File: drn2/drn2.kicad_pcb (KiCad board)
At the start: 2 copper layers, 123 x 89 mm, 54 parts, among them J1 Conn_01x03_Socket, J10 Conn_01x03_Socket, J11 Conn_01x03_Socket, J12 Conn_01x03_Socket, J13 Conn_01x03_Socket, J14 Conn_01x03_Socket, J15 Conn_01x03_Socket, J16 Conn_01x03_Socket, J2 Raspberry_Pi_2_3, J3 Conn_01x03_Socket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

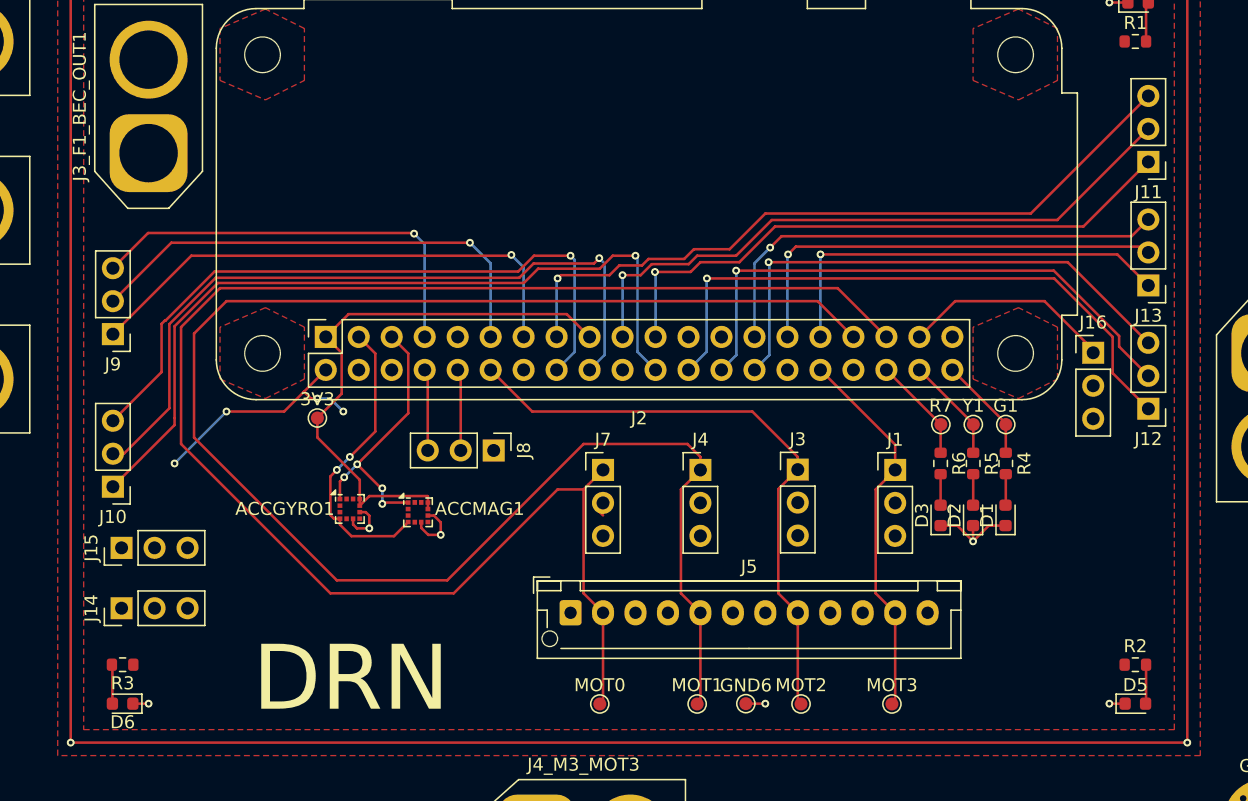
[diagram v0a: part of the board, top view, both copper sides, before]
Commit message: feat: pcb version 2.8
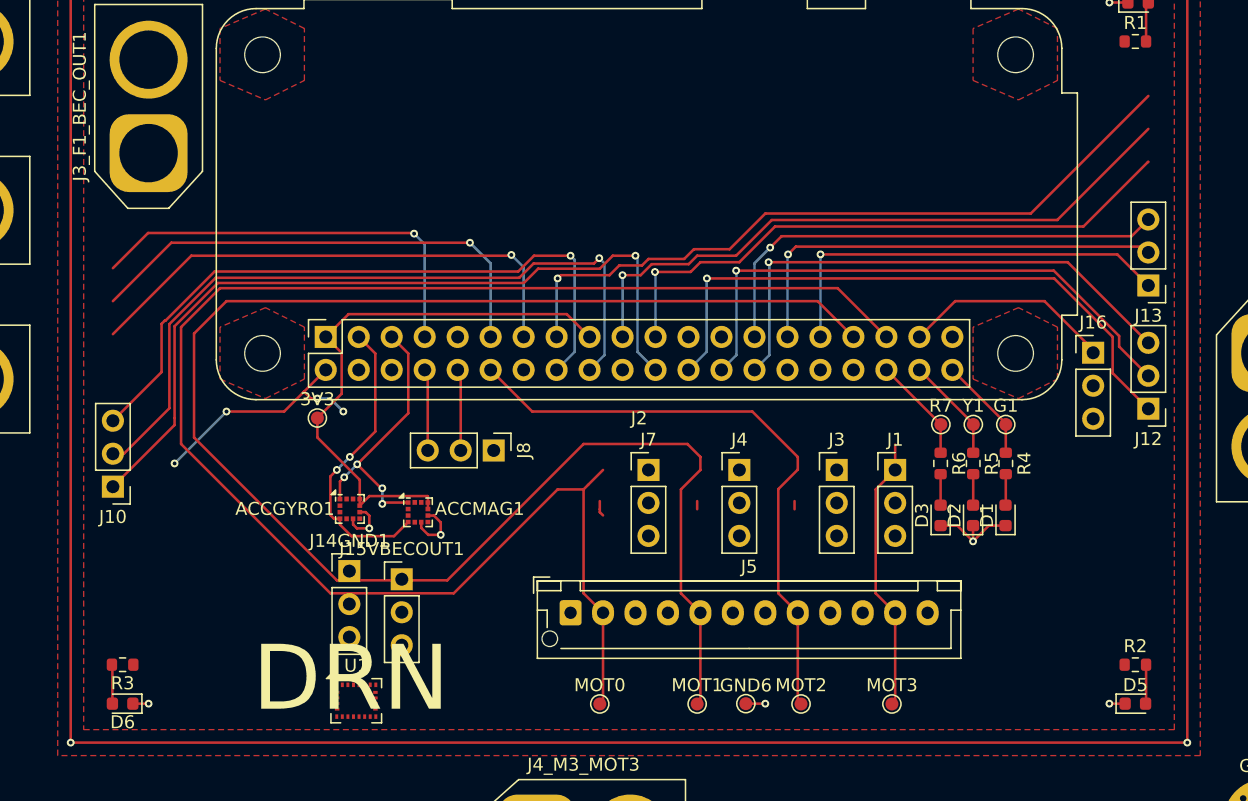
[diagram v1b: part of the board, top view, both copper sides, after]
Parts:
- removed J11, J14, J15, J9: Conn_01x03_Socket, Connector_PinHeader_2.54mm:PinHeader_1x03_P2.54mm_Vertical
- added J14GND1: Conn_01x03_Socket, Connector_PinHeader_2.54mm:PinHeader_1x03_P2.54mm_Vertical, F.Cu at (103.5, 87.8)
- added J15VBECOUT1: Conn_01x03_Socket, Connector_PinHeader_2.54mm:PinHeader_1x03_P2.54mm_Vertical, F.Cu at (107.5, 88.4)
- added U1: LSM9DS1, Package_LGA:LGA-24L_3x3.5mm_P0.43mm, F.Cu at (104.0, 97.8)
- moved J7 3.50 mm to (126.5, 80.0)
- moved J3 3.00 mm to (141.0, 80.0)
- moved J4 3.00 mm to (133.5, 80.0)
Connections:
- J10 pad 1: Net-(J10-Pin_1) -> unconnected-(J10-Pin_1-Pad1)
- J10 pad 2: Net-(J10-Pin_2) -> unconnected-(J10-Pin_2-Pad2)
- J10 pad 3: Net-(J10-Pin_3) -> unconnected-(J10-Pin_3-Pad3)
- J12 pad 1: Net-(J12-Pin_1) -> unconnected-(J12-Pin_1-Pad1)
- J12 pad 2: Net-(J12-Pin_2) -> unconnected-(J12-Pin_2-Pad2)
- J12 pad 3: Net-(J12-Pin_3) -> unconnected-(J12-Pin_3-Pad3)
- J16 pad 1: Net-(J16-Pin_1) -> /GND
- J16 pad 3: /GND -> Net-(J16-Pin_3)
- J2 pad 16: Net-(J10-Pin_3) -> Net-(J2-GPIO23)
- J2 pad 18: Net-(J10-Pin_2) -> Net-(J2-GPIO24)
- J2 pad 22: Net-(J10-Pin_1) -> unconnected-(J2-GPIO25-Pad22)
- J2 pad 23: unconnected-(J2-SCLK0/GPIO11-Pad23) -> Net-(J2-SCLK0/GPIO11)
- J2 pad 24: Net-(J12-Pin_1) -> unconnected-(J2-~{CE0}/GPIO8-Pad24)
- J2 pad 26: Net-(J12-Pin_2) -> unconnected-(J2-~{CE1}/GPIO7-Pad26)
- J2 pad 27: Net-(J13-Pin_3) -> Net-(J13-Pin_1)
- J2 pad 28: Net-(J12-Pin_3) -> unconnected-(J2-ID_SC/GPIO1-Pad28)
- J2 pad 31: Net-(J13-Pin_1) -> Net-(J13-Pin_3)
- J2 pad 32: Net-(J1-Pin_1) -> Net-(J2-PWM0/GPIO12)
- J2 pad 35: Net-(J2-GPIO19/MISO1) -> Net-(J1-Pin_1)
- J2 pad 37: Net-(J16-Pin_1) -> Net-(J16-Pin_3)
- J3 pad 1: Net-(J2-GPIO18/PWM0) -> Net-(J2-PWM1/GPIO13)
- J4 pad 1: Net-(J2-PWM1/GPIO13) -> Net-(J2-PWM0/GPIO12)
- J5 pad 2: Net-(J2-GPIO19/MISO1) -> Net-(J2-GPIO18/PWM0)
- J5 pad 5: Net-(J2-PWM1/GPIO13) -> Net-(J2-PWM0/GPIO12)
- J5 pad 8: Net-(J2-GPIO18/PWM0) -> Net-(J2-PWM1/GPIO13)
- J7 pad 1: Net-(J2-GPIO19/MISO1) -> Net-(J2-GPIO18/PWM0)
- MOT0 pad 1: Net-(J2-GPIO19/MISO1) -> Net-(J1-Pin_1)
- MOT2 pad 1: Net-(J2-GPIO18/PWM0) -> Net-(J2-PWM0/GPIO12)
- MOT3 pad 1: Net-(J1-Pin_1) -> Net-(J2-GPIO18/PWM0)
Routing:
- net (no net): track 0.00 -> 426.8 mm, vias 0 -> 6
- net Net-(J2-GPIO19/MISO1): track 124.6 -> 0.00 mm
- net Net-(J10-Pin_1): track 61.5 -> 0.00 mm, vias 1 -> 0
- net Net-(J10-Pin_2): track 56.7 -> 0.00 mm, vias 1 -> 0
- net Net-(J10-Pin_3): track 52.2 -> 0.00 mm, vias 1 -> 0
- net Net-(J12-Pin_1): track 47.4 -> 0.00 mm, vias 1 -> 0
- net Net-(J12-Pin_2): track 43.7 -> 0.00 mm, vias 1 -> 0
- net Net-(J12-Pin_3): track 40.6 -> 0.00 mm, vias 1 -> 0
- net /GND: track 24.0 -> 40.3 mm
- net Net-(J16-Pin_1): track 16.3 -> 0.00 mm
- net Net-(J1-Pin_1): track 29.5 -> 21.3 mm

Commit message: feat: pcb v3
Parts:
- removed 3V3: TestPoint, TestPoint:TestPoint_Pad_D1.0mm
- removed ACCGYRO1: LSM6, Package_LGA:LGA-12_2x2mm_P0.5mm
- removed ACCMAG1: LSM303, Package_LGA:LGA-12_2x2mm_P0.5mm
- removed J10: Conn_01x03_Socket, Connector_PinHeader_2.54mm:PinHeader_1x03_P2.54mm_Vertical
- added C1: 100nF, Capacitor_SMD:C_0603_1608Metric_Pad1.08x0.95mm_HandSolder, F.Cu at (117.0, 83.5)
- added C2: 100nF, Capacitor_SMD:C_0603_1608Metric_Pad1.08x0.95mm_HandSolder, F.Cu at (118.7, 81.7)
- added C3: 100nF, Capacitor_SMD:C_0603_1608Metric_Pad1.08x0.95mm_HandSolder, F.Cu at (115.0, 83.5)
- added C4: C_Polarized, Capacitor_SMD:CP_Elec_4x5.4, F.Cu at (109.5, 80.5)
- added C5: 10nF, Capacitor_SMD:C_0603_1608Metric_Pad1.08x0.95mm_HandSolder, F.Cu at (113.0, 83.5)
- added R10: 130, Resistor_SMD:R_0603_1608Metric, F.Cu at (110.0, 85.0)
- added R11: 130, Resistor_SMD:R_0603_1608Metric, F.Cu at (121.5, 83.0)
- added R8: 130, Resistor_SMD:R_0603_1608Metric, F.Cu at (106.5, 85.0)
- added R9: 130, Resistor_SMD:R_0603_1608Metric, F.Cu at (121.5, 80.0)
- added VDD1: TestPoint, TestPoint:TestPoint_Pad_D1.0mm, F.Cu at (103.5, 82.4)
- added VDDIO1: TestPoint, TestPoint:TestPoint_Pad_D1.0mm, F.Cu at (125.4, 83.0)
- moved J8 29.5 mm to (89.5, 63.0), turned to 0 degrees
- moved U1 22.2 mm to (115.6, 78.9), turned to 180 degrees
- moved J14GND1 8.89 mm to (111.0, 92.5)
- moved J15VBECOUT1 8.53 mm to (115.0, 92.5)
- moved J7 5.40 mm to (131.9, 80.1)
- moved J13 5.32 mm to (165.0, 60.5), turned to 0 degrees
- moved J16 5.07 mm to (160.8, 76.0), turned to 180 degrees
- moved J12 4.32 mm to (165.0, 71.0), turned to 0 degrees
- moved J4 3.00 mm to (136.5, 80.0)
- moved MOT0 0.25 mm to (145.5, 98.0)
- moved MOT1 0.25 mm to (138.0, 98.0)
- moved MOT2 0.25 mm to (130.5, 98.0)
- moved MOT3 0.25 mm to (123.0, 98.0)
- renumbered MOT3 to MOT0, MOT2 to MOT1, MOT1 to MOT2, MOT0 to MOT3
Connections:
- net /3.3 renamed Net-(J2-3V3-Pad1)
- net /GND renamed GND
- J12 pad 1: unconnected-(J12-Pin_1-Pad1) -> Net-(J12-Pin_1)
- J12 pad 2: unconnected-(J12-Pin_2-Pad2) -> Net-(J12-Pin_2)
- J12 pad 3: unconnected-(J12-Pin_3-Pad3) -> Net-(J12-Pin_3)
- J2 pad 24: unconnected-(J2-~{CE0}/GPIO8-Pad24) -> Net-(J13-Pin_1)
- J2 pad 26: unconnected-(J2-~{CE1}/GPIO7-Pad26) -> Net-(J13-Pin_2)
- J2 pad 27: Net-(J13-Pin_1) -> Net-(J13-Pin_3)
- J2 pad 28: unconnected-(J2-ID_SC/GPIO1-Pad28) -> Net-(J12-Pin_1)
- J2 pad 29: Net-(J13-Pin_2) -> Net-(J12-Pin_2)
- J2 pad 3: Net-(ACCGYRO1-SDA/SDI/SDO) -> Net-(J2-SDA/GPIO2)
- J2 pad 31: Net-(J13-Pin_3) -> Net-(J12-Pin_3)
- J2 pad 5: Net-(ACCGYRO1-SCL/SPC) -> Net-(J2-SCL/GPIO3)
- J3_F1_BEC_OUT1 pad 2: /5V -> unconnected-(J3_F1_BEC_OUT1-Pin_2-Pad2)
- MOT0 pad 1: Net-(J2-GPIO18/PWM0) -> Net-(J1-Pin_1)
- MOT1 pad 1: Net-(J2-PWM0/GPIO12) -> Net-(J2-PWM1/GPIO13)
- MOT2 pad 1: Net-(J2-PWM1/GPIO13) -> Net-(J2-PWM0/GPIO12)
- MOT3 pad 1: Net-(J1-Pin_1) -> Net-(J2-GPIO18/PWM0)
- U1 pad 1: ok -> Net-(C2-Pad2)
- U1 pad 10: Net-(J2-MISO0/GPIO9) -> Net-(J2-GPIO23)
- U1 pad 11: Net-(J2-GPIO17) -> Net-(J2-GPIO27)
- U1 pad 12: Net-(J2-GPIO23) -> Net-(J2-GPIO17)
- U1 pad 13: Net-(J2-GPIO24) -> Net-(J2-GCLK0/GPIO4)
- U1 pad 2: data -> Net-(J2-SCL/GPIO3)
- U1 pad 21: cap -> Net-(U1-CAP)
- U1 pad 22: ok -> Net-(C3-Pad2)
- U1 pad 23: ok -> Net-(C3-Pad2)
- U1 pad 24: cap -> Net-(U1-C1)
- U1 pad 3: ok -> Net-(C2-Pad2)
- U1 pad 4: data -> Net-(J2-SDA/GPIO2)
- U1 pad 5: Net-(J2-GPIO27) -> Net-(J2-SCLK0/GPIO11)
- U1 pad 6: Net-(J2-GCLK0/GPIO4) -> Net-(J2-MISO0/GPIO9)
- U1 pad 7: Net-(J2-GPIO22) -> Net-(J2-MOSI0/GPIO10)
- U1 pad 8: Net-(J2-SCLK0/GPIO11) -> Net-(J2-GPIO24)
- U1 pad 9: Net-(J2-MOSI0/GPIO10) -> Net-(J2-GPIO22)
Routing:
- net (no net): track 426.8 -> 0.00 mm, vias 6 -> 0
- net Net-(J2-PWM1/GPIO13): track 129.7 -> 29.8 mm
- net Net-(J2-GPIO22): track 55.9 -> 11.0 mm, vias 1 -> 0
- net Net-(J12-Pin_1): track 0.00 -> 37.7 mm
- net Net-(J2-MOSI0/GPIO10): track 49.9 -> 12.4 mm, vias 1 -> 0
- net Net-(J12-Pin_2): track 0.00 -> 34.6 mm
- net Net-(J12-Pin_3): track 0.00 -> 33.6 mm
- net Net-(J2-MISO0/GPIO9): track 46.5 -> 14.2 mm, vias 1 -> 0
- net Net-(J2-GPIO27): track 39.9 -> 8.72 mm, vias 1 -> 0
- net Net-(J2-PWM0/GPIO12): track 0.00 -> 29.3 mm
- net Net-(J2-GPIO17): track 37.3 -> 9.07 mm, vias 1 -> 0
- net Net-(ACCGYRO1-SDA/SDI/SDO): track 23.1 -> 0.00 mm, vias 2 -> 0
- net Net-(J2-GCLK0/GPIO4): track 32.6 -> 9.92 mm, vias 1 -> 0
- net Net-(J2-3V3-Pad1): track 43.9 -> 21.8 mm
- net Net-(J2-GPIO15/RXD): track 6.30 -> 27.8 mm, vias 0 -> 1
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
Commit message: feat: new pcb version, removed mess
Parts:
- moved J3_F1_BEC_OUT1 1.12 mm to (87.0, 56.0)
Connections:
- J3_F1_BEC_OUT1 pad 2: unconnected-(J3_F1_BEC_OUT1-Pin_2-Pad2) -> /5V

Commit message: feat: drn pcb v3 almost done
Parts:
- removed G1, GND5, GND6, MOT0, MOT1, MOT2, MOT3, Y1: TestPoint, TestPoint:TestPoint_Pad_D1.0mm
- removed J12, J8: Conn_01x03_Socket, Connector_PinHeader_2.54mm:PinHeader_1x03_P2.54mm_Vertical
- removed J2: Raspberry_Pi_2_3, Module:Raspberry_Pi_Zero_Socketed_THT_FaceDown_MountingHoles
- removed J3_F1_BEC_OUT1, J4_M4_BEC_IN1: Conn_01x02_Pin, Connector_AMASS:AMASS_XT60-F_1x02_P7.20mm_Vertical
- removed J5: Conn_01x12_Socket, Connector_JST:JST_XH_B12B-XH-AM_1x12_P2.50mm_Vertical
- removed J6: Conn_01x08_Socket, Connector_PinHeader_2.54mm:PinHeader_1x08_P2.54mm_Vertical
- added D7: LEDI, LED_SMD:LED_0603_1608Metric, F.Cu at (134.7, 158.5)
- added J10: Conn_01x09_Socket, Connector_PinHeader_2.54mm:PinHeader_1x09_P2.54mm_Vertical, F.Cu at (64.7, 160.9)
- added J9: Conn_01x04_Pin, Connector_JST:JST_XH_B4B-XH-A_1x04_P2.50mm_Vertical, F.Cu at (83.7, 159.8)
- added MO0: TestPoint, TestPoint:TestPoint_Pad_D1.0mm, F.Cu at (131.0, 152.0)
- added MO1: TestPoint, TestPoint:TestPoint_Pad_D1.0mm, F.Cu at (127.0, 152.0)
- added MO2: TestPoint, TestPoint:TestPoint_Pad_D1.0mm, F.Cu at (123.0, 152.0)
- added MO3: TestPoint, TestPoint:TestPoint_Pad_D1.0mm, F.Cu at (119.0, 152.0)
- added R14: 300K, Resistor_SMD:R_0603_1608Metric, F.Cu at (68.0, 151.7)
- added R15: 100k, Resistor_SMD:R_0603_1608Metric, F.Cu at (68.0, 148.7)
- added RPI02: Raspberry_Pi_2_3, Module:Raspberry_Pi_Zero_Socketed_THT_FaceDown_MountingHoles, F.Cu at (86.9, 140.1)
- added SCL1: TestPoint, TestPoint:TestPoint_Pad_D1.0mm, F.Cu at (97.6, 151.4)
- added SDA3: TestPoint, TestPoint:TestPoint_Pad_D1.0mm, F.Cu at (95.0, 151.4)
- added TXRX1: Conn_01x03_Socket, Connector_PinHeader_2.54mm:PinHeader_1x03_P2.54mm_Vertical, F.Cu at (92.0, 146.9)
- added U3: MCP3004, Package_DIP:DIP-14_W7.62mm, F.Cu at (70.6, 154.1)
- J13: value Conn_01x03_Socket -> Conn_01x04_Socket; footprint Connector_PinHeader_2.54mm:PinHeader_1x03_P2.54mm_Vertical -> Connector_PinHeader_2.54mm:PinHeader_1x04_P2.54mm_Vertical
- R7: value TestPoint -> 130; footprint TestPoint:TestPoint_Pad_D1.0mm -> Resistor_SMD:R_0603_1608Metric
- moved GND4 146.9 mm to (150.6, 179.0)
- moved GND3 145.7 mm to (71.2, 179.6)
- moved J4_M1_MOT1 135.5 mm to (106.4, 170.0)
- moved GND7 130.7 mm to (151.8, 160.2)
- moved 5V1 127.7 mm to (148.2, 160.5)
- moved J3_F2_BAT1 123.0 mm to (69.4, 170.0)
- moved J4_M2_MOT2 110.7 mm to (124.8, 170.0), turned to 0 degrees
- moved GND2 108.4 mm to (71.3, 141.6)
- moved J13 102.2 mm to (113.2, 148.6), turned to 90 degrees
- moved J4_M0_MOT0 99.2 mm to (88.0, 170.0)
- moved BAT1 95.8 mm to (64.8, 178.4)
- moved D4 94.0 mm to (157.8, 137.8)
- moved R1 92.6 mm to (157.8, 139.4)
- moved GND1 91.4 mm to (151.2, 142.6)
- moved R3 88.6 mm to (64.6, 181.0)
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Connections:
- J1 pad 1: Net-(J1-Pin_1) -> GND
- J1 pad 3: GND -> Net-(J1-Pin_3)
- J13 pad 1: Net-(J13-Pin_1) -> GND
- J3 pad 1: Net-(J2-PWM1/GPIO13) -> GND
- J3 pad 3: GND -> Net-(J3-Pin_3)
- J4 pad 1: Net-(J2-PWM0/GPIO12) -> GND
- J4 pad 3: GND -> Net-(J4-Pin_3)
- J7 pad 1: Net-(J2-GPIO18/PWM0) -> GND
- J7 pad 3: GND -> Net-(J7-Pin_3)
- R6 pad 1: Net-(J2-GPIO16) -> Net-(RPI02-GPIO16)
- R7 pad 1: Net-(J2-GPIO16) -> /5V
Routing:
- net GND: track 31.7 -> 303.7 mm, vias 22 -> 23
- net /11.1: track 0.00 -> 144.2 mm
- net Net-(J2-GPIO18/PWM0): track 46.2 -> 0.00 mm, vias 1 -> 0
- net Net-(RPI02-SCLK0/GPIO11): track 0.00 -> 43.6 mm, vias 0 -> 2
- net Net-(J13-Pin_1): track 41.3 -> 0.00 mm
- net Net-(RPI02-MISO0/GPIO9): track 0.00 -> 37.9 mm, vias 0 -> 2
- net /5V: track 3.17 -> 40.9 mm, vias 0 -> 4
- net Net-(J12-Pin_1): track 37.7 -> 0.00 mm
- net Net-(J12-Pin_2): track 34.6 -> 0.00 mm
- net Net-(J12-Pin_3): track 33.6 -> 0.00 mm
- net Net-(RPI02-MOSI0/GPIO10): track 0.00 -> 32.3 mm, vias 0 -> 2
- net Net-(RPI02-GPIO16): track 0.00 -> 32.1 mm, vias 0 -> 2
- net Net-(J7-Pin_3): track 0.00 -> 31.5 mm, vias 0 -> 2
- net Net-(RPI02-~{CE0}/GPIO8): track 0.00 -> 30.7 mm, vias 0 -> 2
- net Net-(J1-Pin_1): track 30.6 -> 0.00 mm
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- added copper zone on In1.Cu, net /11.1
- added copper zone on In1.Cu, net /5V
- added copper zone on In2.Cu, net GND
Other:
- board size 123 x 89 mm -> 96.8 x 46.8 mm
- copper layers 2 -> 4
- board text removed: "DRN"
- board text removed: "HIGH VOLTAGE"

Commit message: drn v4
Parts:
- removed J10: Conn_01x09_Socket, Connector_PinHeader_2.54mm:PinHeader_1x09_P2.54mm_Vertical
- removed J13: Conn_01x04_Socket, Connector_PinHeader_2.54mm:PinHeader_1x04_P2.54mm_Vertical
- removed J14GND1, J15VBECOUT1, J16, TXRX1: Conn_01x03_Socket, Connector_PinHeader_2.54mm:PinHeader_1x03_P2.54mm_Vertical
- removed RPI02: Raspberry_Pi_2_3, Module:Raspberry_Pi_Zero_Socketed_THT_FaceDown_MountingHoles
- removed U1: LSM9DS1, Package_LGA:LGA-24L_3x3.5mm_P0.43mm
- removed U3: MCP3004, Package_DIP:DIP-14_W7.62mm
- added 5V2: TestPoint, TestPoint:TestPoint_Pad_D1.0mm, F.Cu at (133.2, 158.0)
- added GND5: MountingHole_Pad, MountingHole:MountingHole_3.2mm_M3_Pad_Via, F.Cu at (151.7, 148.1)
- added I2C1: Conn_01x04_Socket, Connector_PinHeader_2.54mm:PinHeader_1x04_P2.54mm_Vertical, F.Cu at (72.1, 161.2)
- added IMU1: LSM9DS1, Package_LGA:LGA-24L_3x3.5mm_P0.43mm, F.Cu at (102.9, 157.7)
- added J2: Conn_01x04_Socket, Connector_PinSocket_2.54mm:PinSocket_1x04_P2.54mm_Vertical, F.Cu at (68.4, 161.2)
- added J37: Conn_01x03_Socket, Connector_PinHeader_2.54mm:PinHeader_1x03_P2.54mm_Vertical, F.Cu at (157.0, 153.5)
- added MAN1: ADS1115IDGS, Package_SO:TSSOP-10_3x3mm_P0.5mm, F.Cu at (88.2, 154.4)
- added RPI2: Raspberry_Pi_2_3, Module:Raspberry_Pi_Zero_Socketed_THT_FaceDown_MountingHoles, F.Cu at (87.1, 146.8)
- added SPI1: Conn_01x04_Socket, Connector_PinHeader_2.54mm:PinHeader_1x04_P2.54mm_Vertical, F.Cu at (72.0, 153.7)
- added TOF1: Conn_01x04_Socket, Connector_PinHeader_2.54mm:PinHeader_1x04_P2.54mm_Vertical, F.Cu at (125.7, 161.0)
- added UART1: Conn_01x04_Socket, Connector_PinHeader_2.54mm:PinHeader_1x04_P2.54mm_Vertical, F.Cu at (72.1, 157.4)
- 5V1: value TestPoint -> Conn_01x03_Socket; footprint TestPoint:TestPoint_Pad_D1.0mm -> Connector_PinHeader_2.54mm:PinHeader_1x03_P2.54mm_Vertical
- GND1: value MountingHole_Pad -> Conn_01x03_Socket; footprint MountingHole:MountingHole_3.2mm_M3_Pad_Via -> Connector_PinHeader_2.54mm:PinHeader_1x03_P2.54mm_Vertical
- R14: value 300K -> 7K5
- R15: value 100k -> 2K5
- moved D3 43.6 mm to (119.3, 161.5), turned to 90 degrees
- moved R6 41.7 mm to (119.3, 158.5), turned to -90 degrees
- moved D2 35.5 mm to (120.8, 161.5), turned to 90 degrees
- moved D1 33.2 mm to (122.3, 161.5), turned to 90 degrees
- moved R5 31.0 mm to (120.8, 158.5), turned to -90 degrees
- moved R4 28.5 mm to (122.3, 158.5), turned to -90 degrees
- moved D7 21.2 mm to (113.5, 159.0)
- moved R7 21.2 mm to (113.5, 160.6)
- moved GND7 21.0 mm to (131.0, 158.0)
- moved J7 18.0 mm to (137.0, 161.0)
- moved J4 17.8 mm to (140.8, 161.0)
- moved J3 17.5 mm to (144.5, 161.0)
- moved J1 17.3 mm to (148.2, 161.0)
- moved R15 17.0 mm to (83.9, 154.7)
- moved MO3 16.1 mm to (135.1, 153.2)
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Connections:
- C1 pad 1: Net-(U1-C1) -> GND
- C1 pad 2: GND -> Net-(IMU1-C1)
- C5 pad 1: Net-(U1-CAP) -> GND
- C5 pad 2: GND -> Net-(IMU1-CAP)
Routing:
- net Net-(RPI02-SCLK0/GPIO11): track 43.6 -> 0.00 mm, vias 2 -> 0
- net Net-(RPI02-MISO0/GPIO9): track 37.9 -> 0.00 mm, vias 2 -> 0
- net Net-(RPI02-MOSI0/GPIO10): track 32.3 -> 0.00 mm, vias 2 -> 0
- net Net-(RPI2-GPIO16): track 32.1 -> 0.00 mm, vias 2 -> 0
- net Net-(RPI02-~{CE0}/GPIO8): track 30.7 -> 0.00 mm, vias 2 -> 0
- net Net-(J7-Pin_3): track 31.5 -> 3.60 mm, vias 2 -> 1
- net Net-(J16-Pin_3): track 24.4 -> 0.00 mm, vias 2 -> 0
- net Net-(MAN1-AIN3): track 37.3 -> 13.0 mm
- net Net-(RPI02-ID_SD/GPIO0): track 23.9 -> 0.00 mm
- net Net-(MAN1-AIN2): track 34.0 -> 10.1 mm, vias 0 -> 2
- net Net-(J37-Pin_3): track 0.00 -> 23.0 mm
- net Net-(RPI02-ID_SC/GPIO1): track 21.9 -> 0.00 mm
- net Net-(RPI02-3V3-Pad1): track 21.3 -> 0.00 mm
- net Net-(RPI02-~{CE1}/GPIO7): track 19.8 -> 0.00 mm
- net Net-(RPI2-GCLK1/GPIO5): track 0.00 -> 18.2 mm
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- removed copper zone on F.Cu, net GND
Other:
- board size 96.8 x 46.8 mm -> 96.8 x 39.8 mm

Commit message: v4 done, requires FP check
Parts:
- moved J3_F2_BAT1 42.8 mm to (112.2, 170.2), turned to -90 degrees
- moved D3 29.5 mm to (148.8, 160.1), turned to 180 degrees
- moved D2 28.1 mm to (148.8, 158.6), turned to 180 degrees
- moved R4 27.6 mm to (149.4, 153.1)
- moved R5 27.6 mm to (147.9, 153.1)
- moved R6 27.6 mm to (146.4, 153.1)
- moved D1 26.8 mm to (148.8, 157.1), turned to 180 degrees
- moved J4_M3_MOT3 22.9 mm to (127.8, 186.8), turned to 180 degrees
- moved J4_M1_MOT1 19.6 mm to (96.5, 186.8)
- moved 5V2 18.1 mm to (149.1, 149.3)
- moved GND7 17.7 mm to (146.3, 149.2)
- moved GND3 14.6 mm to (83.5, 187.8)
- moved BAT1 14.6 mm to (77.0, 186.3)
- moved D6 14.0 mm to (76.1, 190.6)
- moved R3 14.0 mm to (76.1, 188.9)
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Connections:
- RPI2 pad 15: Net-(IMU1-INT_M) -> Net-(IMU1-DRDY_M)
- RPI2 pad 16: Net-(IMU1-DRDY_M) -> Net-(IMU1-INT_M)
- SPI1 pad 2: Net-(RPI2-MOSI0/GPIO10) -> Net-(RPI2-MISO0/GPIO9)
- SPI1 pad 3: Net-(RPI2-MISO0/GPIO9) -> Net-(RPI2-MOSI0/GPIO10)
- TOF1 pad 2: Net-(RPI2-GCLK1/GPIO5) -> Net-(RPI2-GCLK2/GPIO6)
- TOF1 pad 3: Net-(RPI2-GCLK2/GPIO6) -> Net-(RPI2-GCLK1/GPIO5)
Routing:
- net /11.1: track 144.2 -> 0.90 mm
- net GND: track 286.2 -> 404.9 mm, vias 21 -> 11
- net Net-(RPI2-MISO0/GPIO9): track 0.00 -> 37.6 mm
- net /5V: track 41.0 -> 78.4 mm, vias 4 -> 15
- net Net-(I2C1-Pin_2): track 18.9 -> 55.9 mm, vias 0 -> 4
- net Net-(MAN1-AIN0): track 0.00 -> 35.3 mm, vias 0 -> 2
- net Net-(I2C1-Pin_3): track 16.2 -> 50.5 mm, vias 0 -> 3
- net Net-(RPI2-MOSI0/GPIO10): track 0.00 -> 31.8 mm
- net Net-(MAN1-ALERT/RDY): track 0.00 -> 27.7 mm, vias 0 -> 2
- net Net-(MAN1-ADDR): track 0.00 -> 25.2 mm, vias 0 -> 2
- net Net-(J7-Pin_3): track 3.60 -> 27.4 mm
- net Net-(IMU1-DEN_A/G): track 0.00 -> 20.4 mm
- net Net-(RPI2-GPIO15/RXD): track 0.00 -> 16.5 mm
- net Net-(RPI2-GPIO14/TXD): track 0.00 -> 16.5 mm
- net Net-(IMU1-INT2_A/G): track 0.00 -> 16.3 mm
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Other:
- board size 96.8 x 39.8 mm -> 76.2 x 70 mm
- board text added: "DRN"
- board text added: "G/5V"
- board text added: "HOT SURFACE"
- board text added: "Made with and by Ekter v4"
- board text added: "V/IO"
- board text added: "Warning! High current, PCB can get hot!"
- board text added: "github:ekter/drn"
